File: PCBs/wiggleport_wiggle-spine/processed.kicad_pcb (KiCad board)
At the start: 2 copper layers, 88.9 x 114.3 mm, 190 parts, among them CON1 USB-B, CON2 XLR-3 Female, CON3 USB-A, CON4 2.5mm 5-24V 5A, CON5 5-24V 16A, CON6 PLR135, CON7 PLT133, Q1 DMN3190LDW, Q2 2N7002P, Q3 AOD4189, T1 10/100baseT transformer, U1 93C56, U10 SiP32408, U11 SiP32408, U12 TCR2EF25, U13 TCR2EF12, U14 Si5351B, U2 FT2232H, U3 NC7WZ14, U4 AP2204K-5.0, U5 ST485E, U6 iCE40-HX1K-TQ144, U7 RT8299A, U8 RT8299A, U9 SiP32408, X1 12 MHz, X2 25.0000 MHz 15ppm 8pF

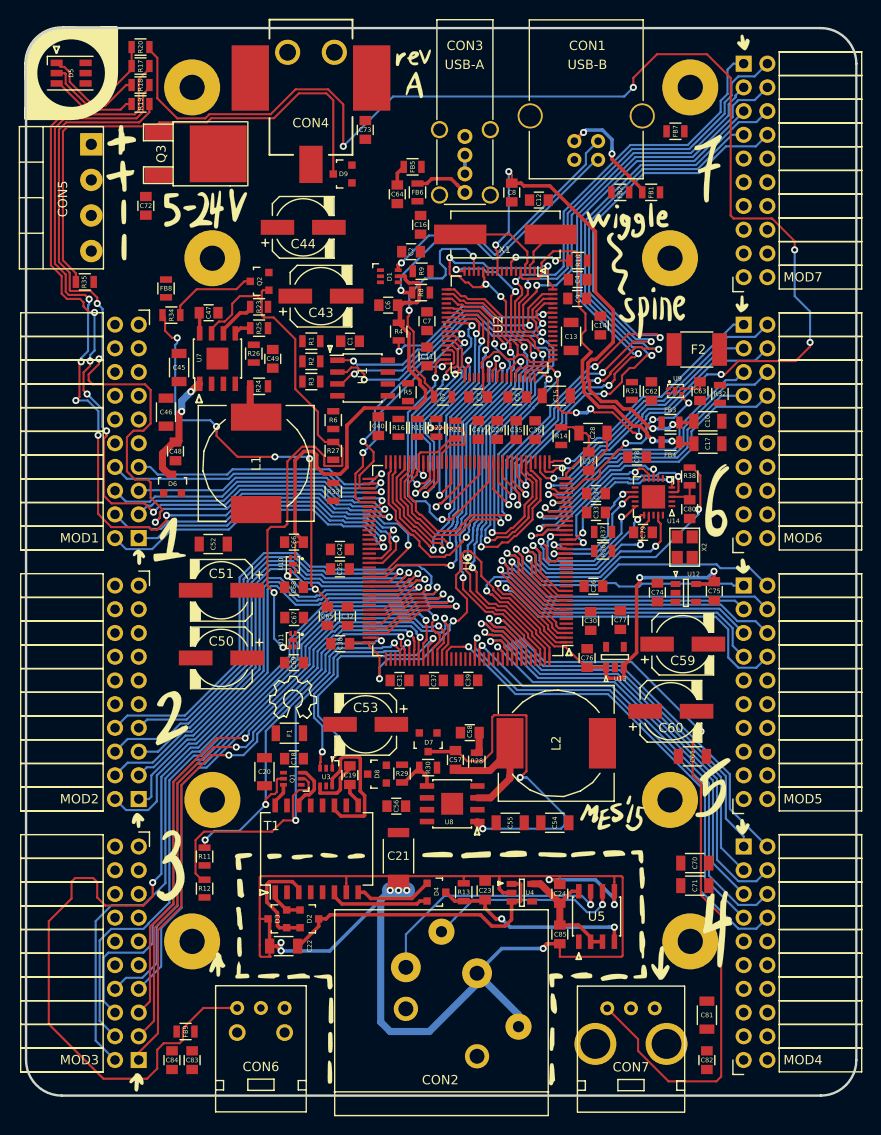
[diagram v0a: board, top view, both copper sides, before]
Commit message: recheck all circuits and clean up fill zone by rerouting the nets using freerouting and manually
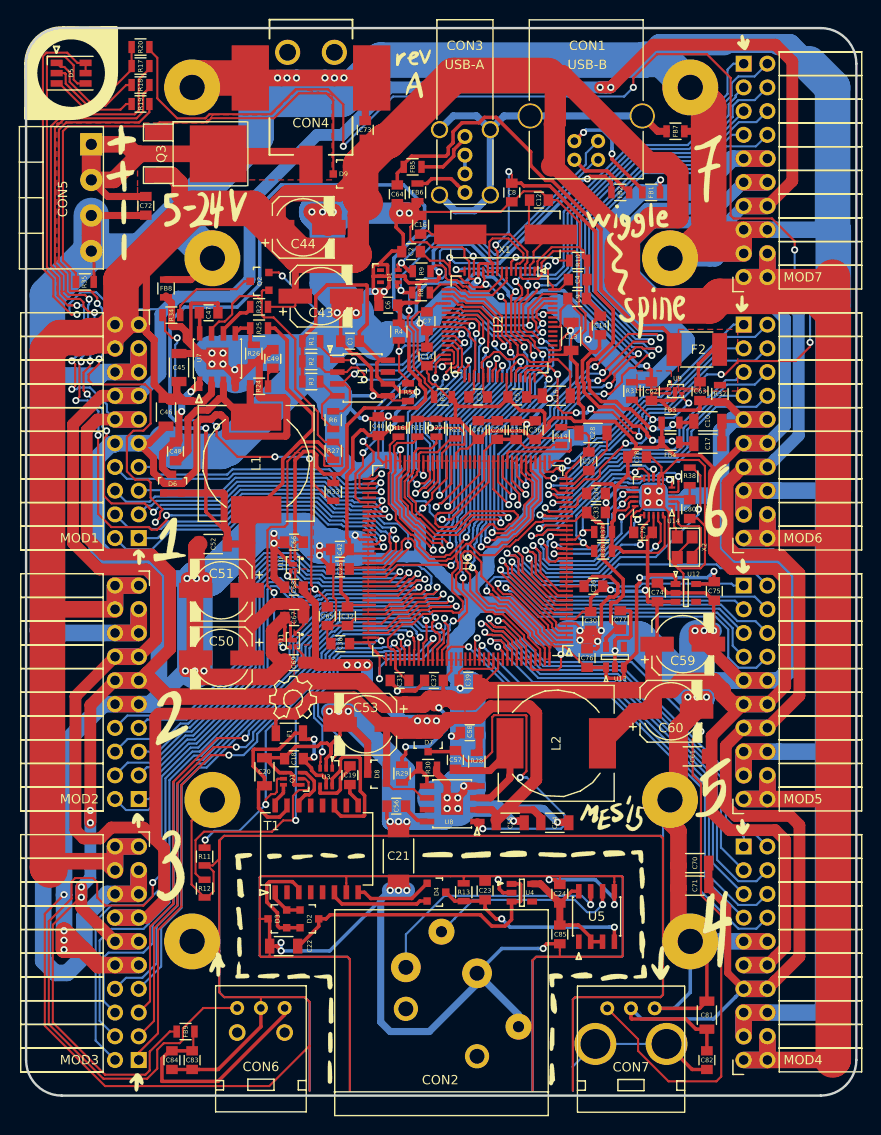
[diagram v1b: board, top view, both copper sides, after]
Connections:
- C1 pad 1: (no net) -> GND
- C1 pad 2: (no net) -> +3V3
- C10 pad 2: (no net) -> GND
- C11 pad 1: (no net) -> GND
- C11 pad 2: (no net) -> +3V3
- C12 pad 1: (no net) -> GND
- C12 pad 2: (no net) -> Net-(C12-Pad2)
- C13 pad 1: (no net) -> +3V3
- C13 pad 2: (no net) -> GND
- C14 pad 1: (no net) -> GND
- C14 pad 2: (no net) -> /USB/FTDI_VPHY
- C15 pad 1: (no net) -> /USB/FTDI_1V8REG
- C15 pad 2: (no net) -> GND
- C16 pad 1: (no net) -> GND
- C16 pad 2: (no net) -> Net-(C16-Pad2)
- C17 pad 2: (no net) -> GND
- C18 pad 1: (no net) -> GND
- C18 pad 2: (no net) -> Net-(C18-Pad2)
- C2 pad 1: (no net) -> GND
- C2 pad 2: (no net) -> /USB/FTDI_1V8REG
- C20 pad 1: (no net) -> Net-(C18-Pad2)
- C20 pad 2: (no net) -> GND
- C21 pad 2: (no net) -> GND
- C25 pad 1: (no net) -> GND
- C25 pad 2: (no net) -> +1V2
- C26 pad 1: (no net) -> GND
- C26 pad 2: (no net) -> +3V3
- C29 pad 1: (no net) -> GND
- C29 pad 2: (no net) -> +1V2
- C3 pad 1: (no net) -> GND
- C30 pad 1: (no net) -> GND
- C30 pad 2: (no net) -> +3V3
- C31 pad 1: (no net) -> GND
- C31 pad 2: (no net) -> +1V2
- C32 pad 1: (no net) -> GND
- C32 pad 2: (no net) -> +3V3
- C33 pad 1: (no net) -> GND
- C33 pad 2: (no net) -> +1V2
- C34 pad 1: (no net) -> GND
- C34 pad 2: (no net) -> +3V3
- C35 pad 1: (no net) -> GND
- C35 pad 2: (no net) -> +1V2
- C36 pad 1: (no net) -> GND
- C36 pad 2: (no net) -> +3V3
- C37 pad 1: (no net) -> GND
- C37 pad 2: (no net) -> +3V3
- C38 pad 1: (no net) -> GND
- C39 pad 1: (no net) -> GND
- C39 pad 2: (no net) -> +3V3
- C4 pad 1: (no net) -> GND
- C4 pad 2: (no net) -> /USB/FTDI_1V8REG
- C40 pad 1: (no net) -> GND
- C40 pad 2: (no net) -> +3V3
- C41 pad 1: (no net) -> GND
- C41 pad 2: (no net) -> +3V3
- C42 pad 1: (no net) -> GND
- C42 pad 2: (no net) -> +3V3
- C43 pad 1: (no net) -> +24V
- C43 pad 2: (no net) -> GND
- C44 pad 1: (no net) -> +24V
- C44 pad 2: (no net) -> GND
- C45 pad 1: (no net) -> +24V
- C45 pad 2: (no net) -> GND
- C46 pad 1: (no net) -> +24V
- C46 pad 2: (no net) -> GND
- C47 pad 2: (no net) -> GND
- C48 pad 1: (no net) -> Net-(C48-Pad1)
- C48 pad 2: (no net) -> Net-(C48-Pad2)
- C49 pad 1: (no net) -> GND
- C49 pad 2: (no net) -> Net-(C49-Pad2)
- C5 pad 1: (no net) -> GND
- C5 pad 2: (no net) -> +3V3
- C50 pad 1: (no net) -> /Power/USB Power Output/5V_IN
- C50 pad 2: (no net) -> GND
- C51 pad 1: (no net) -> /Power/USB Power Output/5V_IN
- C51 pad 2: (no net) -> GND
- C52 pad 1: (no net) -> /Power/USB Power Output/5V_IN
- C52 pad 2: (no net) -> GND
- C53 pad 1: (no net) -> +5V
- C53 pad 2: (no net) -> GND
- C54 pad 1: (no net) -> +5V
- C54 pad 2: (no net) -> GND
- C55 pad 1: (no net) -> +5V
- C55 pad 2: (no net) -> GND
- C56 pad 1: (no net) -> Net-(C56-Pad1)
- C56 pad 2: (no net) -> GND
- C58 pad 1: (no net) -> GND
- C59 pad 1: (no net) -> +3V3
- C59 pad 2: (no net) -> GND
- C6 pad 1: (no net) -> GND
- C60 pad 1: (no net) -> +3V3
- C60 pad 2: (no net) -> GND
- C61 pad 1: (no net) -> +3V3
- C61 pad 2: (no net) -> GND
- C62 pad 1: (no net) -> /Power/USB Power Output/5V_IN
- C62 pad 2: (no net) -> GND
- C63 pad 1: (no net) -> GND
- C64 pad 1: (no net) -> GND
- C65 pad 1: (no net) -> GND
- C66 pad 2: (no net) -> GND
- C67 pad 1: (no net) -> /Power/USB Power Output/5V_IN
- C67 pad 2: (no net) -> GND
- C68 pad 1: (no net) -> GND
- C68 pad 2: (no net) -> +5V
- C69 pad 1: (no net) -> GND
- C69 pad 2: (no net) -> +5V
- C7 pad 1: (no net) -> GND
- C7 pad 2: (no net) -> +3V3
- C70 pad 1: (no net) -> +5V
- C70 pad 2: (no net) -> GND
- C71 pad 1: (no net) -> +5V
- C71 pad 2: (no net) -> GND
- C72 pad 1: (no net) -> GNDPWR
- C72 pad 2: (no net) -> /Power/5-24V Power Input/POWER_IN
- C73 pad 1: (no net) -> +24V
- C73 pad 2: (no net) -> GNDPWR
- C74 pad 1: (no net) -> GND
- C74 pad 2: (no net) -> +3V3
- C75 pad 2: (no net) -> GND
- C76 pad 1: (no net) -> GND
- C77 pad 1: (no net) -> +1V2
- C77 pad 2: (no net) -> GND
- C78 pad 1: (no net) -> GND
- C78 pad 2: (no net) -> +3V3
- C79 pad 1: (no net) -> GND
- C79 pad 2: (no net) -> +3V3
- C8 pad 1: (no net) -> GND
- C80 pad 2: (no net) -> GND
- C81 pad 1: (no net) -> +5V
- C81 pad 2: (no net) -> GND
- C82 pad 1: (no net) -> GND
- C82 pad 2: (no net) -> +5V
- C83 pad 1: (no net) -> GND
- C83 pad 2: (no net) -> Net-(C83-Pad2)
- C84 pad 1: (no net) -> Net-(C83-Pad2)
- C84 pad 2: (no net) -> GND
- C9 pad 1: (no net) -> GND
- C9 pad 2: (no net) -> +3V3
- CON1 pad 1: (no net) -> Net-(CON1-Pad1)
- CON1 pad 5: (no net) -> Earth
- CON3 pad 1: (no net) -> Net-(CON3-Pad1)
- CON3 pad 5: (no net) -> Earth
- CON4 pad 1: (no net) -> /Power/5-24V Power Input/POWER_IN
- CON4 pad 2: (no net) -> GNDPWR
- CON4 pad 3: (no net) -> GNDPWR
- CON5 pad 1: (no net) -> /Power/5-24V Power Input/POWER_IN
- CON5 pad 2: (no net) -> /Power/5-24V Power Input/POWER_IN
- CON5 pad 3: (no net) -> GNDPWR
- CON5 pad 4: (no net) -> GNDPWR
- CON6 pad 1: (no net) -> Net-(C83-Pad2)
- CON6 pad 2: (no net) -> GND
- CON7 pad 1: (no net) -> GND
- CON7 pad 2: (no net) -> +5V
- D1 pad 2: (no net) -> GND
- D1 pad 4: (no net) -> Net-(CON1-Pad2)
- D5 pad 4: (no net) -> +3V3
- D5 pad 5: (no net) -> +5V
- D5 pad 6: (no net) -> +5V
- D6 pad 1: (no net) -> /Power/USB Power Output/5V_IN
- D6 pad 2: (no net) -> /Power/USB Power Output/5V_IN
- D7 pad 1: (no net) -> +5V
- D7 pad 2: (no net) -> +5V
- D8 pad 1: (no net) -> +5V
- D8 pad 2: (no net) -> +5V
- D8 pad 3: (no net) -> GND
- D9 pad 1: (no net) -> +24V
- D9 pad 2: (no net) -> +24V
- F1 pad 1: (no net) -> Net-(C18-Pad2)
- F1 pad 2: (no net) -> +5V
- F2 pad 1: (no net) -> Net-(C63-Pad2)
- F2 pad 2: (no net) -> Net-(C64-Pad2)
- FB1 pad 1: (no net) -> GND
- FB2 pad 1: (no net) -> Net-(CON1-Pad1)
- FB2 pad 2: (no net) -> /Power/VBUS_UPSTREAM
- FB3 pad 1: (no net) -> +3V3
- FB4 pad 1: (no net) -> +3V3
- FB5 pad 2: (no net) -> Net-(CON3-Pad1)
- FB6 pad 1: (no net) -> GND
- FB7 pad 1: (no net) -> GNDPWR
- FB7 pad 2: (no net) -> Earth
- FB8 pad 1: (no net) -> GNDPWR
- FB8 pad 2: (no net) -> GND
- FB9 pad 1: (no net) -> +3V3
- FB9 pad 2: (no net) -> Net-(C83-Pad2)
- L1 pad 2: (no net) -> /Power/USB Power Output/5V_IN
- L2 pad 2: (no net) -> +3V3
- MOD1 pad 10: (no net) -> GND
- MOD1 pad 11: (no net) -> +3V3
- MOD1 pad 12: (no net) -> +3V3
- MOD1 pad 13: (no net) -> +5V
- MOD1 pad 14: (no net) -> +5V
- MOD1 pad 15: (no net) -> GNDPWR
- MOD1 pad 16: (no net) -> GNDPWR
- MOD1 pad 17: (no net) -> GNDPWR
- MOD1 pad 18: (no net) -> +24V
- MOD1 pad 19: (no net) -> +24V
- MOD1 pad 20: (no net) -> +24V
- MOD1 pad 9: (no net) -> GND
- MOD2 pad 10: (no net) -> GND
- MOD2 pad 11: (no net) -> +3V3
- MOD2 pad 12: (no net) -> +3V3
- MOD2 pad 13: (no net) -> +5V
- MOD2 pad 14: (no net) -> +5V
- MOD2 pad 15: (no net) -> GNDPWR
- MOD2 pad 16: (no net) -> GNDPWR
- MOD2 pad 17: (no net) -> GNDPWR
- MOD2 pad 18: (no net) -> +24V
- MOD2 pad 19: (no net) -> +24V
- MOD2 pad 20: (no net) -> +24V
- MOD2 pad 9: (no net) -> GND
- MOD3 pad 10: (no net) -> GND
- MOD3 pad 11: (no net) -> +3V3
- MOD3 pad 12: (no net) -> +3V3
- MOD3 pad 13: (no net) -> +5V
- MOD3 pad 14: (no net) -> +5V
- MOD3 pad 15: (no net) -> GNDPWR
- MOD3 pad 16: (no net) -> GNDPWR
- MOD3 pad 17: (no net) -> GNDPWR
- MOD3 pad 18: (no net) -> +24V
- MOD3 pad 19: (no net) -> +24V
- MOD3 pad 20: (no net) -> +24V
- MOD3 pad 9: (no net) -> GND
- MOD4 pad 10: (no net) -> GND
- MOD4 pad 11: (no net) -> +3V3
- MOD4 pad 12: (no net) -> +3V3
- MOD4 pad 13: (no net) -> +5V
- MOD4 pad 14: (no net) -> +5V
- MOD4 pad 15: (no net) -> GNDPWR
- MOD4 pad 16: (no net) -> GNDPWR
- MOD4 pad 17: (no net) -> GNDPWR
- MOD4 pad 18: (no net) -> +24V
- MOD4 pad 19: (no net) -> +24V
- MOD4 pad 20: (no net) -> +24V
- MOD4 pad 9: (no net) -> GND
- MOD5 pad 10: (no net) -> GND
- MOD5 pad 11: (no net) -> +3V3
- MOD5 pad 12: (no net) -> +3V3
- MOD5 pad 13: (no net) -> +5V
- MOD5 pad 14: (no net) -> +5V
- MOD5 pad 15: (no net) -> GNDPWR
- MOD5 pad 16: (no net) -> GNDPWR
- MOD5 pad 17: (no net) -> GNDPWR
- MOD5 pad 18: (no net) -> +24V
- MOD5 pad 19: (no net) -> +24V
- MOD5 pad 20: (no net) -> +24V
- MOD5 pad 9: (no net) -> GND
- MOD6 pad 10: (no net) -> GND
- MOD6 pad 11: (no net) -> +3V3
- MOD6 pad 12: (no net) -> +3V3
- MOD6 pad 13: (no net) -> +5V
- MOD6 pad 14: (no net) -> +5V
- MOD6 pad 15: (no net) -> GNDPWR
- MOD6 pad 16: (no net) -> GNDPWR
- MOD6 pad 17: (no net) -> GNDPWR
- MOD6 pad 18: (no net) -> +24V
- MOD6 pad 19: (no net) -> +24V
- MOD6 pad 20: (no net) -> +24V
- MOD6 pad 9: (no net) -> GND
- MOD7 pad 10: (no net) -> GND
- MOD7 pad 11: (no net) -> +3V3
- MOD7 pad 12: (no net) -> +3V3
- MOD7 pad 13: (no net) -> +5V
- MOD7 pad 14: (no net) -> +5V
- MOD7 pad 15: (no net) -> GNDPWR
- MOD7 pad 16: (no net) -> GNDPWR
- MOD7 pad 17: (no net) -> GNDPWR
- MOD7 pad 18: (no net) -> +24V
- MOD7 pad 19: (no net) -> +24V
- MOD7 pad 20: (no net) -> +24V
- MOD7 pad 9: (no net) -> GND
- Q1 pad 1: (no net) -> GND
- Q1 pad 4: (no net) -> GND
- Q2 pad 2: (no net) -> GND
- Q3 pad 1: (no net) -> Net-(D9-Pad3)
- Q3 pad 2: (no net) -> /Power/5-24V Power Input/POWER_IN
- Q3 pad 3: (no net) -> +24V
- R1 pad 1: (no net) -> /USB/EECS
- R1 pad 2: (no net) -> +3V3
- R10 pad 1: (no net) -> GND
- R11 pad 2: (no net) -> GND
- R12 pad 2: (no net) -> GND
- R14 pad 2: (no net) -> +1V2
- R15 pad 1: (no net) -> /USB/SPI_CLK
- R15 pad 2: (no net) -> +3V3
- R16 pad 1: (no net) -> GND
- R16 pad 2: (no net) -> /USB/GPIO_L0
- R2 pad 1: (no net) -> /USB/EECLK
- R2 pad 2: (no net) -> +3V3
- R21 pad 2: (no net) -> +3V3
- R22 pad 1: (no net) -> /FPGA/CRESET_B
- R22 pad 2: (no net) -> +3V3
- R23 pad 1: (no net) -> +24V
- R24 pad 1: (no net) -> Net-(C49-Pad2)
- R25 pad 2: (no net) -> /Power/USB Power Output/5V_IN
- R26 pad 1: (no net) -> GND
- R26 pad 2: (no net) -> Net-(R25-Pad1)
- R27 pad 2: (no net) -> /Power/USB Power Output/5V_IN
- R29 pad 2: (no net) -> +3V3
- R3 pad 1: (no net) -> /USB/EEDATA_OUT
- R3 pad 2: (no net) -> +3V3
- R30 pad 1: (no net) -> GND
- R30 pad 2: (no net) -> Net-(R29-Pad1)
- R31 pad 1: (no net) -> /FPGA/VBUS_DOWNSTREAM_EN
- R31 pad 2: (no net) -> /Power/USB Power Output/5V_IN
- R32 pad 1: (no net) -> Net-(C63-Pad2)
- R32 pad 2: (no net) -> GND
- R33 pad 1: (no net) -> /Power/VBUS_UPSTREAM
- R33 pad 2: (no net) -> Net-(C65-Pad2)
- R35 pad 2: (no net) -> GNDPWR
- R36 pad 1: (no net) -> +3V3
- R36 pad 2: (no net) -> /FPGA/CLK_SCL
- R37 pad 1: (no net) -> +3V3
- R37 pad 2: (no net) -> /FPGA/CLK_SDA
- R5 pad 1: (no net) -> GND
- R5 pad 2: (no net) -> /USB/VBUS_SENSE
- R6 pad 1: (no net) -> /USB/EEDATA_OUT
- R6 pad 2: (no net) -> /USB/EEDATA
- R7 pad 2: (no net) -> +3V3
- R8 pad 2: (no net) -> Net-(R8-Pad2)
- R9 pad 1: (no net) -> Net-(CON1-Pad3)
- R9 pad 2: (no net) -> Net-(R9-Pad2)
- REF** pad 1: (no net) -> GND (x4)
- REF** pad 1: (no net) -> GNDPWR (x4)
- T1 pad 15: (no net) -> Net-(C18-Pad2)
- U1 pad 4: (no net) -> /USB/EEDATA_OUT
- U1 pad 5: (no net) -> GND
- U1 pad 6: (no net) -> +3V3
- U1 pad 8: (no net) -> +3V3
- U10 pad 2: (no net) -> GND
- U10 pad 4: (no net) -> +5V
- U10 pad 5: (no net) -> GND
- U11 pad 1: (no net) -> /Power/USB Power Output/5V_IN
- U11 pad 2: (no net) -> GND
- U11 pad 4: (no net) -> +5V
- U11 pad 5: (no net) -> GND
- U12 pad 1: (no net) -> +3V3
- U12 pad 2: (no net) -> GND
- U12 pad 3: (no net) -> +3V3
- U13 pad 2: (no net) -> GND
- U13 pad 5: (no net) -> +1V2
- U14 pad 1: (no net) -> Net-(U14-Pad1)
- U14 pad 10: (no net) -> +3V3
- U14 pad 11: (no net) -> +3V3
- U14 pad 14: (no net) -> +3V3
- U14 pad 18: (no net) -> +3V3
- U14 pad 2: (no net) -> Net-(U14-Pad2)
- U14 pad 20: (no net) -> +3V3
- U14 pad 21: (no net) -> GND
- U14 pad 6: (no net) -> GND
- U14 pad 7: (no net) -> GND
- U2 pad 1: (no net) -> GND
- U2 pad 10: (no net) -> GND
- U2 pad 11: (no net) -> GND
- U2 pad 13: (no net) -> GND
- U2 pad 15: (no net) -> GND
- U2 pad 20: (no net) -> +3V3
- U2 pad 25: (no net) -> GND
- U2 pad 31: (no net) -> +3V3
- U2 pad 35: (no net) -> GND
- U2 pad 42: (no net) -> +3V3
- U2 pad 47: (no net) -> GND
- U2 pad 5: (no net) -> GND
- U2 pad 50: (no net) -> +3V3
- U2 pad 51: (no net) -> GND
- U2 pad 56: (no net) -> +3V3
- U2 pad 7: (no net) -> Net-(R8-Pad2)
- U2 pad 8: (no net) -> Net-(R9-Pad2)
- U3 pad 2: (no net) -> GND
- U3 pad 5: (no net) -> Net-(C18-Pad2)
- U6 pad 100: (no net) -> +3V3
- U6 pad 103: (no net) -> GND
- U6 pad 111: (no net) -> +1V2
- U6 pad 123: (no net) -> +3V3
- U6 pad 13: (no net) -> GND
- U6 pad 132: (no net) -> GND
- U6 pad 133: (no net) -> +3V3
- U6 pad 14: (no net) -> GND
- U6 pad 140: (no net) -> GND
- U6 pad 27: (no net) -> +1V2
- U6 pad 30: (no net) -> +3V3
- U6 pad 35: (no net) -> Net-(C27-Pad1)
- U6 pad 46: (no net) -> +3V3
- U6 pad 5: (no net) -> GND
- U6 pad 51: (no net) -> +1V2
- U6 pad 57: (no net) -> +3V3
- U6 pad 59: (no net) -> GND
- U6 pad 6: (no net) -> +3V3
- U6 pad 69: (no net) -> GND
- U6 pad 72: (no net) -> +3V3
- U6 pad 86: (no net) -> GND
- U6 pad 89: (no net) -> +3V3
- U6 pad 92: (no net) -> +1V2
- U7 pad 2: (no net) -> +24V
- U7 pad 3: (no net) -> Net-(C48-Pad1)
- U7 pad 4: (no net) -> GND
- U7 pad 9: (no net) -> GND
- U8 pad 2: (no net) -> +5V
- U8 pad 4: (no net) -> GND
- U8 pad 6: (no net) -> +5V
- U8 pad 8: (no net) -> Net-(C56-Pad1)
- U8 pad 9: (no net) -> GND
- U9 pad 1: (no net) -> /Power/USB Power Output/5V_IN
- U9 pad 2: (no net) -> GND
- U9 pad 5: (no net) -> GND
- X2 pad 1: (no net) -> Net-(U14-Pad1)
- X2 pad 2: (no net) -> GND
- X2 pad 3: (no net) -> Net-(U14-Pad2)
- X2 pad 4: (no net) -> GND
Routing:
- net GND: track 0.00 -> 1690.6 mm, vias 0 -> 76
- net +3V3: track 0.00 -> 699.3 mm, vias 0 -> 13
- net +5V: track 0.00 -> 588.4 mm, vias 0 -> 9
- net GNDPWR: track 0.00 -> 540.4 mm, vias 0 -> 6
- net +24V: track 0.00 -> 484.6 mm
- net /Power/USB Power Output/5V_IN: track 0.00 -> 195.3 mm, vias 0 -> 2
- net /DMX512/DMXGND: track 165.2 -> 308.7 mm, vias 8 -> 9
- net +1V2: track 0.00 -> 111.5 mm
- net Net-(C64-Pad2): track 2.22 -> 49.2 mm
- net /Power/5-24V Power Input/POWER_IN: track 0.00 -> 44.8 mm
- net Earth: track 0.00 -> 40.7 mm
- net /Power/VBUS_UPSTREAM: track 55.0 -> 87.5 mm, vias 0 -> 2
- net Net-(C18-Pad2): track 0.00 -> 26.3 mm, vias 0 -> 2
- net Net-(C83-Pad2): track 0.00 -> 24.8 mm
- net Net-(C48-Pad1): track 3.57 -> 19.4 mm
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- added copper zone on F.Cu, net +1V2
- added copper zone on F.Cu, net +3V3
- added copper zone on F.Cu, net +5V
- added copper zone on F.Cu, net /Power/5-24V Power Input/POWER_IN
- added copper zone on F.Cu, net /Power/USB Power Output/5V_IN
- added copper zone on F.Cu, net /Power/VBUS_UPSTREAM
- added copper zone on F.Cu, net Net-(C63-Pad2)

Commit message: clean psbc that are missed before
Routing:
- removed copper zone on F.Cu, net +1V2
- removed copper zone on F.Cu, net +3V3
- removed copper zone on F.Cu, net /Power/5-24V Power Input/POWER_IN

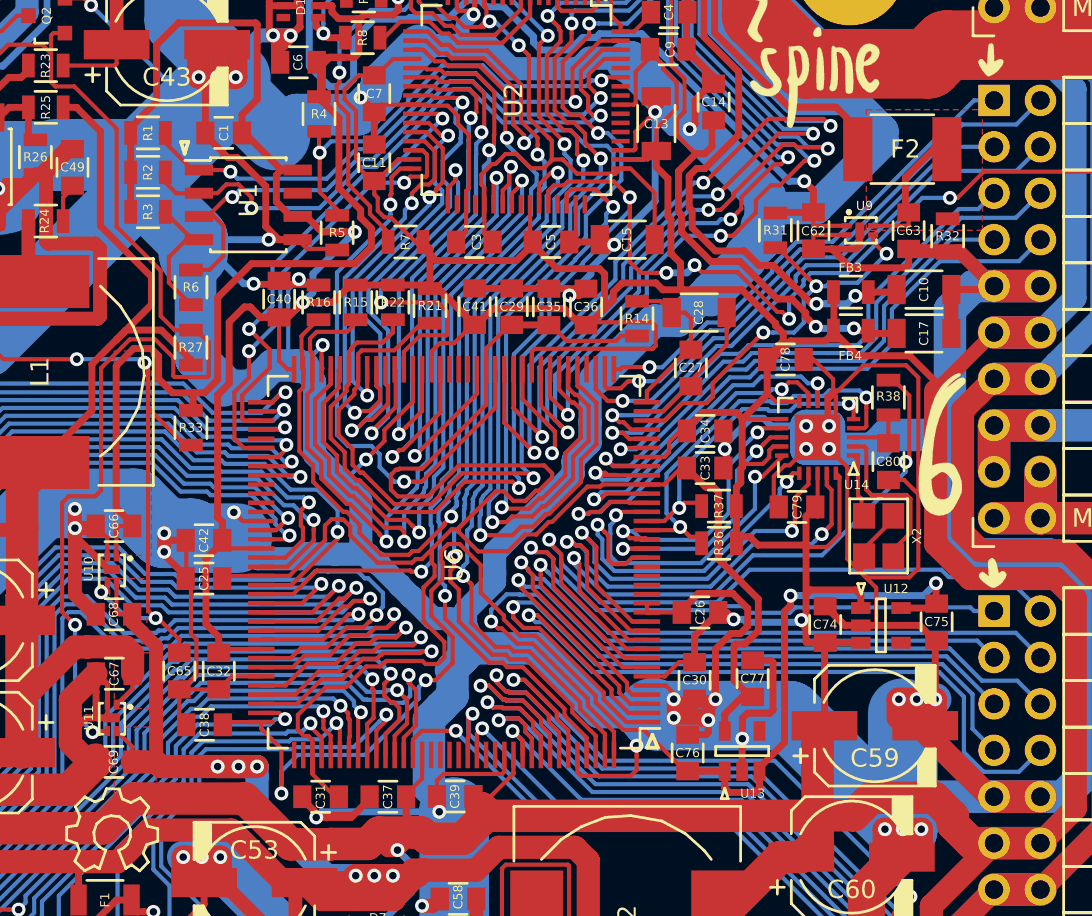
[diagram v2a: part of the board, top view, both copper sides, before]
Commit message: add wires to replace fill zones of wiggle pcb
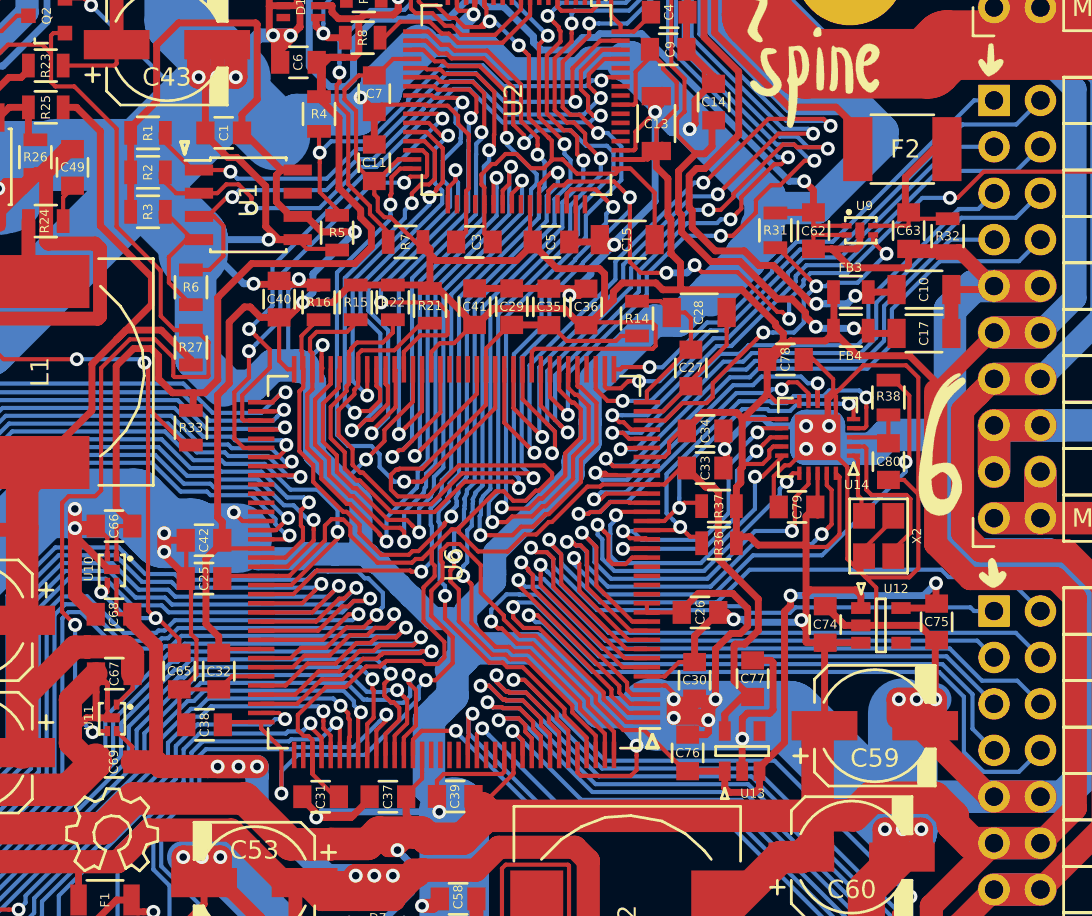
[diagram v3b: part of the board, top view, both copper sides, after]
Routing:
- net Net-(C63-Pad2): track 6.90 -> 9.18 mm
- removed copper zone on F.Cu, net +5V
- removed copper zone on F.Cu, net /Power/USB Power Output/5V_IN
- removed copper zone on F.Cu, net /Power/VBUS_UPSTREAM
- removed copper zone on F.Cu, net Net-(C63-Pad2)
